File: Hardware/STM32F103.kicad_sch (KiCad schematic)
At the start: 20 parts, among them J2 Conn_02x03_Odd_Even, J3 Conn_02x04_Counter_Clockwise, SW3 SW_Push, U1 STM32F103C8Tx, U9 LD1117, Y1 8Mhz

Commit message: Update Sche
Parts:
- removed C10: 100nF, IVS_FOOTPRINTS:C_0603, symbol IVS_SYMBOLS:C
- removed C11: 10uF, IVS_FOOTPRINTS:C_0603, symbol IVS_SYMBOLS:C
- removed R24: 120R, IVS_FOOTPRINTS:R_0603, symbol IVS_SYMBOLS:R
- removed U1: STM32F103C8Tx, Package_QFP:LQFP-48_7x7mm_P0.5mm, symbol MCU_ST_STM32F1:STM32F103C8Tx
- removed U9: LD1117, IVS_FOOTPRINTS:SOT233, symbol IVS_SYMBOLS:LD1117
- added J9: Conn_01x04, Connector_PinHeader_2.54mm:PinHeader_1x04_P2.54mm_Vertical, symbol IVS_SYMBOLS:Conn_01x04
- added U5: MCU_STM32F103C8Tx, IVS_FOOTPRINTS:LQFP-48_7x7mm_P0.5mm, symbol IVS_SYMBOLS:MCU_STM32F103C8Tx
- J3: footprint (none) -> Connector_PinHeader_2.54mm:PinHeader_2x04_P2.54mm_Vertical
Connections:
- net GND: now also J9.4 (Pin_4), U5.23 (VSS), U5.35 (VSS), U5.47 (VSS), U5.8 (VSSA)
- net OSC_IN: now also U5.5 (PD0/OSC_IN)
- net OSC_OUT: now also U5.6 (PD1/OSC_OUT)
- net RST: now also U5.7 (NRST)
- net RX_LOG: now also U5.22 (PB11/I2C2_SDA/USART3_RX/TIM2_CH4)
- net SWCLK: now also U5.37 (PA14/JTCK/SWCLK)
- net SWDIO: now also U5.34 (PA13/JTMS/SWDIO)
- net TX_LOG: now also U5.21 (PB10/I2C2_SCL/USART3_TX/TIM2_CH3)
- net VBAT: now also U5.1 (VBAT)
- net at R13.2: now also U5.20 (PB2/BOOT1)
- net at R14.2: now also U5.44 (BOOT0)
- net +3V3 renamed +3V3_MCU
- net +3V3_MCU: now also U5.24 (VDD), U5.36 (VDD), U5.48 (VDD), U5.9 (VDDA)
- net +5V renamed +5VA
- net +5VA: now also J9.1 (Pin_1)
- new net CAN_RX: J9.2 (Pin_2), U5.32 (PA11/USART1_CTS/CANRX/USBDM/TIM1_CH4)
- new net CAN_TX: J9.3 (Pin_3), U5.33 (PA12/USART1_RTS/CANTX/USBDP/TIM1_ETR)
- new net MCU_PWM1: U5.16 (PA6/SPI1_MISO/ADC12_IN6/TIM3_CH1)
- new net MCU_PWM2: U5.17 (PA7/SPI1_MOSI/ADC12_IN7/TIM3_CH2)
- new net MCU_PWM3: U5.18 (PB0/ADC12_IN8/TIM3_CH3/TIM1_CH2N)
- new net MCU_PWM4: U5.19 (PB1/ADC12_IN9/TIM3_CH4/TIM1_CH3N)
- new net MCU_PWM_BLDC: U5.11 (PA1/USART2_RTS/ADC12_IN1/TIM2_CH2)
- new net MCU_SCL: U5.45 (PB8/TIM4_CH3/I2C1_SCL/CANRX)
- new net MCU_SDA: U5.46 (PB9/TIM4_CH4/I2C1_SDA/CANTX)

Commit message: Add cap 10uF and 100nF of LD1117
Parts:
- C10, C11, C12, C13, C14, C15, C16: footprint IVS_FOOTPRINTS:C0603 -> IVS_FOOTPRINTS:C_0603
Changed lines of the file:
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@@
       (effects (font (size 1.27 1.27)) (justify right))
     )
-    (property "Footprint" "IVS_FOOTPRINTS:C0603" (at 199.6948 123.19 0)
+    (property "Footprint" "IVS_FOOTPRINTS:C_0603" (at 199.6948 123.19 0)
       (effects (font (size 1.27 1.27)) hide)
     )
@@
       (effects (font (size 1.27 1.27)) (justify left))
     )
-    (property "Footprint" "IVS_FOOTPRINTS:C0603" (at 223.2152 106.68 0)
+    (property "Footprint" "IVS_FOOTPRINTS:C_0603" (at 223.2152 106.68 0)
       (effects (font (size 1.27 1.27)) hide)
     )
@@
       (effects (font (size 1.27 1.27)))
     )
-    (property "Footprint" "IVS_FOOTPRINTS:C0603" (at 234.95 128.5748 0)
+    (property "Footprint" "IVS_FOOTPRINTS:C_0603" (at 234.95 128.5748 0)
       (effects (font (size 1.27 1.27)) hide)
     )
@@
       (effects (font (size 1.27 1.27)) (justify left))
     )
-    (property "Footprint" "IVS_FOOTPRINTS:C0603" (at 261.3152 106.68 0)
+    (property "Footprint" "IVS_FOOTPRINTS:C_0603" (at 261.3152 106.68 0)
       (effects (font (size 1.27 1.27)) hide)
     )
@@
       (effects (font (size 1.27 1.27)))
     )
-    (property "Footprint" "IVS_FOOTPRINTS:C0603" (at 255.27 128.5748 0)
+    (property "Footprint" "IVS_FOOTPRINTS:C_0603" (at 255.27 128.5748 0)
       (effects (font (size 1.27 1.27)) hide)
     )
@@
       (effects (font (size 1.27 1.27)) (justify left))
     )
-    (property "Footprint" "IVS_FOOTPRINTS:C0603" (at 248.6152 106.68 0)
+    (property "Footprint" "IVS_FOOTPRINTS:C_0603" (at 248.6152 106.68 0)
       (effects (font (size 1.27 1.27)) hide)
     )
@@
       (effects (font (size 1.27 1.27)) (justify left))
     )
-    (property "Footprint" "IVS_FOOTPRINTS:C0603" (at 235.9152 106.68 0)
-      (effects (font (size 1.27 1.27)) hide)
-    )
+    (property "Footprint" "IVS_FOOTPRINTS:C_0603" (at 235.9152 106.68 0)
+      (effects (font (size 1.27 1.27)) hide)
+    )

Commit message: Up schematic
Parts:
- removed J9: Conn_01x04, Connector_PinHeader_2.54mm:PinHeader_1x04_P2.54mm_Vertical, symbol IVS_SYMBOLS:Conn_01x04
- added LE2: Led, IVS_FOOTPRINTS:LED_0603, symbol IVS_SYMBOLS:Led
- added R14: 2K2, IVS_FOOTPRINTS:R0603, symbol Thu_vien_kicad:R
- U5: footprint IVS_FOOTPRINTS:LQFP-48_7x7mm_P0.5mm -> IVS_FOOTPRINTS:Package-IC-LQFP-48P-7x7mm-P0.5mm
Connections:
- net +3V3_MCU: now also J3.7 (Pin_7), LE2.1; no longer J3.4 (Pin_4)
- net +5VA: now also J3.8 (Pin_8); no longer J3.5 (Pin_5)
- net GND: now also J3.5 (Pin_5); no longer J3.3 (Pin_3)
- net RX_LOG: now also J3.2 (Pin_2); no longer J3.8 (Pin_8)
- net SWDIO: now also J3.3 (Pin_3); no longer J3.2 (Pin_2)
- net TX_LOG: now also J3.4 (Pin_4); no longer J3.7 (Pin_7)
- net PWM_R2: now reaches U5.10 (PA0/WKUP/USART2_CTS/ADC12_IN0/TIM2_CH1_ETR)
- net PWM_R1: now reaches U5.12 (PA2/USART2_TX/ADC12_IN2/TIM2_CH3)
- net PWM_L1: now reaches U5.13 (PA3/USART2_RX/ADC12_IN3/TIM2_CH4)
- net at U5.2 (PC13/TAMPER-RTC): now also R14.2
- net MCU_En1_A: now reaches U5.42 (PB6/USART1_TX/I2C1_SCL/TIM4_CH1)
- net MCU_En1_B: now reaches U5.43 (PB7/USART1_RX/I2C1_SDA/TIM4_CH2)
- net CAN_RX: no longer names the net of U5.32 (PA11/USART1_CTS/CANRX/USBDM/TIM1_CH4)
- net CAN_TX: no longer names the net of U5.33 (PA12/USART1_RTS/CANTX/USBDP/TIM1_ETR)
- net MCU_PWM1 renamed MCU_En2_A
- net MCU_PWM2 renamed MCU_En2_B
- net MCU_PWM3: no longer names the net of U5.18 (PB0/ADC12_IN8/TIM3_CH3/TIM1_CH2N)
- net MCU_PWM4: no longer names the net of U5.19 (PB1/ADC12_IN9/TIM3_CH4/TIM1_CH3N)
- net MCU_PWM_BLDC renamed PWM_L2
- net MCU_SCL: no longer names the net of U5.45 (PB8/TIM4_CH3/I2C1_SCL/CANRX)
- net MCU_SDA: no longer names the net of U5.46 (PB9/TIM4_CH4/I2C1_SDA/CANTX)
- new net: LE2.2, R14.1

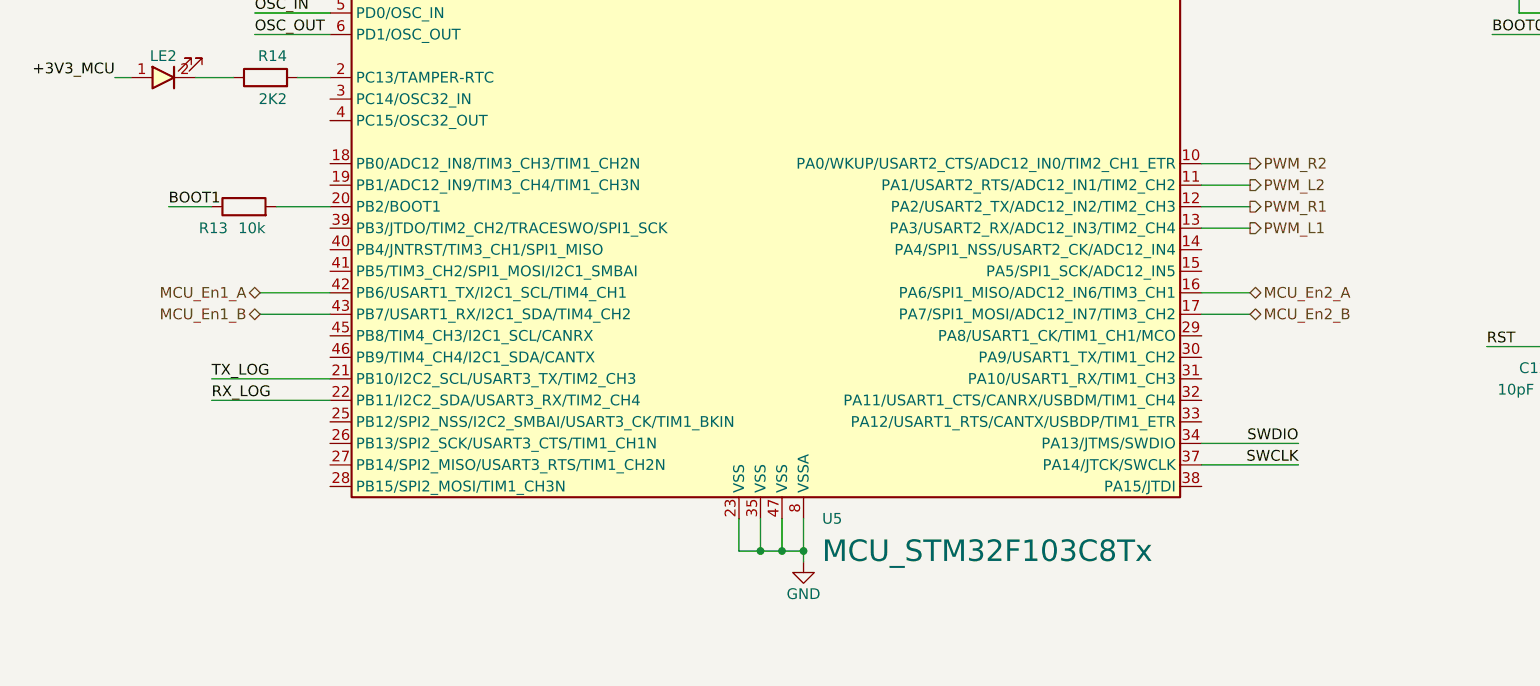
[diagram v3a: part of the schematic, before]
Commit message: Update schematic part2
Vẽ bus dành cho khối BLDC
Đóng khối chức năng cho sheet MCT8316
Tạo sheet nguồn cho các mạch nguồn Buck DCDC, LDO LD1117, BS0505
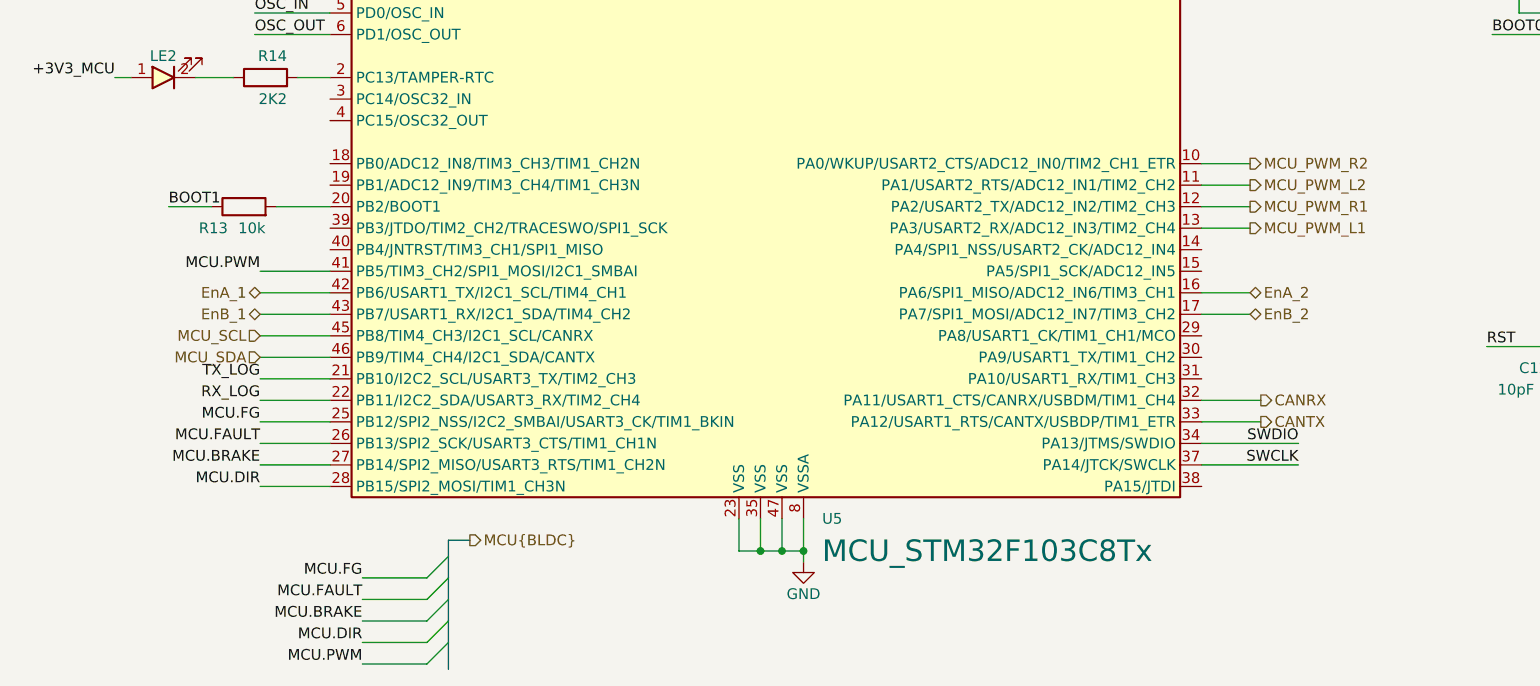
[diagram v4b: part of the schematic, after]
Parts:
- J3: footprint Connector_PinHeader_2.54mm:PinHeader_2x04_P2.54mm_Vertical -> Connector_IDC:IDC-Header_2x04_P2.54mm_Vertical
- R13, R14, R41, R9: footprint IVS_FOOTPRINTS:R0603 -> IVS_FOOTPRINTS:R_0603
- SW3: footprint IVS_FOOTPRINTS:SW_SPST_PTS810 -> IVS_FOOTPRINTS:ButtonPush-Vert-SMD-4P-SPST_PTS810
- Y1: footprint IVS_FOOTPRINTS:Crystal_SMD_3225-4Pin_3.2x2.5mm -> IVS_FOOTPRINTS:Crystal-SMD-4P-3.2x2.6mm-3225
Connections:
- net MCU.FG: now reaches U5.25 (PB12/SPI2_NSS/I2C2_SMBAI/USART3_CK/TIM1_BKIN)
- net MCU.FAULT: now reaches U5.26 (PB13/SPI2_SCK/USART3_CTS/TIM1_CH1N)
- net MCU.BRAKE: now reaches U5.27 (PB14/SPI2_MISO/USART3_RTS/TIM1_CH2N)
- net MCU.DIR: now reaches U5.28 (PB15/SPI2_MOSI/TIM1_CH3N)
- net CANRX: now reaches U5.32 (PA11/USART1_CTS/CANRX/USBDM/TIM1_CH4)
- net CANTX: now reaches U5.33 (PA12/USART1_RTS/CANTX/USBDP/TIM1_ETR)
- net MCU.PWM: now reaches U5.41 (PB5/TIM3_CH2/SPI1_MOSI/I2C1_SMBAI)
- net MCU_SCL: now reaches U5.45 (PB8/TIM4_CH3/I2C1_SCL/CANRX)
- net MCU_SDA: now reaches U5.46 (PB9/TIM4_CH4/I2C1_SDA/CANTX)
- net MCU_En1_A renamed EnA_1
- net MCU_En1_B renamed EnB_1
- net MCU_En2_A renamed EnA_2
- net MCU_En2_B renamed EnB_2
- net PWM_L1 renamed MCU_PWM_L1
- net PWM_L2 renamed MCU_PWM_L2
- net PWM_R1 renamed MCU_PWM_R1
- net PWM_R2 renamed MCU_PWM_R2

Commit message: Add PCB
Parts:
- removed J2: Conn_02x03_Odd_Even, Connector_PinHeader_2.54mm:PinHeader_2x03_P2.54mm_Vertical, symbol Connector_Generic:Conn_02x03_Odd_Even
- added S2: SolderJump3P, Jumper:SolderJumper-3_P1.3mm_Open_RoundedPad1.0x1.5mm_NumberLabels, symbol IVS_SYMBOLS:EG1206
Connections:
- net BOOT0 is gone; now on net GND: R14.1
- net BOOT1 is gone; now on net GND: R13.1
- net MCU.PWM: now also S2.3; no longer U5.41 (PB5/TIM3_CH2/SPI1_MOSI/I2C1_SMBAI)
- net MCU_PWM_R1: now also S2.1; no longer U5.12 (PA2/USART2_TX/ADC12_IN2/TIM2_CH3)
- net VBAT: no longer names the net of U5.1 (VBAT)
- new net MCU_PA2: S2.2, U5.12 (PA2/USART2_TX/ADC12_IN2/TIM2_CH3)
- no-connect marks 0 -> 1
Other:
- note added: "CRYSTAL"
- note added: "Coupling capacitor"
- note added: "HEADER"
- note added: "MCU STM32F103C8T6"
- note added: "RESET"
- moved on the sheet: C10, C11, C12, C13, C14, C15, C16, J3, LE2, R13, R14, R41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

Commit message: Layout PCB
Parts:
- added C12: 10uF, IVS_FOOTPRINTS:C_0603, symbol Thu_vien_kicad:C
- added J8: Conn_01x03_Pin, IVS_FOOTPRINTS:Conn-Vert-THT-3P-2.54mm-S3B_XH_SM4_TB, symbol IVS_SYMBOLS:Conn_01x03_Pin
- added R10, R24: 4k7, IVS_FOOTPRINTS:R_0603, symbol IVS_SYMBOLS:R
- added R14 (x2): 1K, IVS_FOOTPRINTS:R_0603, symbol Thu_vien_kicad:R
- added S2: SolderJump3P, Jumper:SolderJumper-3_P1.3mm_Open_RoundedPad1.0x1.5mm_NumberLabels, symbol IVS_SYMBOLS:EG1206
- added U13: EL817, IVS_FOOTPRINTS:OptoIsolation-EL357N-G, symbol IVS_SYMBOLS:EL817
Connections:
- net +3V3_MCU: now also R10.1, R24.1, U13.4
- net GND: now also R14.1
- net MCU.BRAKE: now also U5.14 (PA4/SPI1_NSS/USART2_CK/ADC12_IN4); no longer U5.27 (PB14/SPI2_MISO/USART3_RTS/TIM1_CH2N)
- net MCU.DIR: now also S2.3; no longer U5.28 (PB15/SPI2_MOSI/TIM1_CH3N)
- net EnA_1 renamed MCU.EnA_1
- net EnA_2 renamed MCU.EnA_2
- net EnB_1 renamed MCU.EnB_1
- net EnB_2 renamed MCU.EnB_2
- net MCU_PA2 renamed MCU.PWM_R1
- net MCU.PWM_R1: no longer S2.2
- net MCU_PWM_L1 renamed MCU.PWM_L1
- net MCU_PWM_L2 renamed MCU_PA1
- net MCU_PA1: now also S2.2
- net MCU_PWM_R1 renamed MCU.PWM_L2
- net MCU_PWM_R2 renamed MCU_PA0
- net MCU_PA0: now also S2.2
- net MCU_SCL renamed MCU.SCL
- net MCU.SCL: now also R10.2
- net MCU_SDA renamed MCU.SDA
- net MCU.SDA: now also R24.2
- new net: C12.1, J8.2 (Pin_2)
- new net: J8.3 (Pin_3), R14.1
- new net: R14.2, U13.3
- new net: R14.2, U13.1
- new net +24V_CS: C12.2, J8.1 (Pin_1)
- new net GNDD: U13.2
- new net MCU.PWM_R2: S2.1
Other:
- moved on the sheet: S2

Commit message: Update components
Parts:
- removed C12: 10uF, IVS_FOOTPRINTS:C_0603, symbol Thu_vien_kicad:C
- removed J8: Conn_01x03_Pin, IVS_FOOTPRINTS:Conn-Vert-THT-3P-2.54mm-S3B_XH_SM4_TB, symbol IVS_SYMBOLS:Conn_01x03_Pin
- removed R14 (x2): 1K, IVS_FOOTPRINTS:R_0603, symbol Thu_vien_kicad:R
- removed U13: EL817, IVS_FOOTPRINTS:OptoIsolation-EL357N-G, symbol IVS_SYMBOLS:EL817
